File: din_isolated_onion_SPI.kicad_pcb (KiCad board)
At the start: 2 copper layers, 32.5 x 40.5 mm, 38 parts, among them J1 Conn_01x16, J2 Conn_01x16, J3 Conn_01x10, U1 Omega2+, U2 SI8661AB-B-IS1, U3 TPL5010-Q1, U4 74LVC125, U5 NL7SZ19

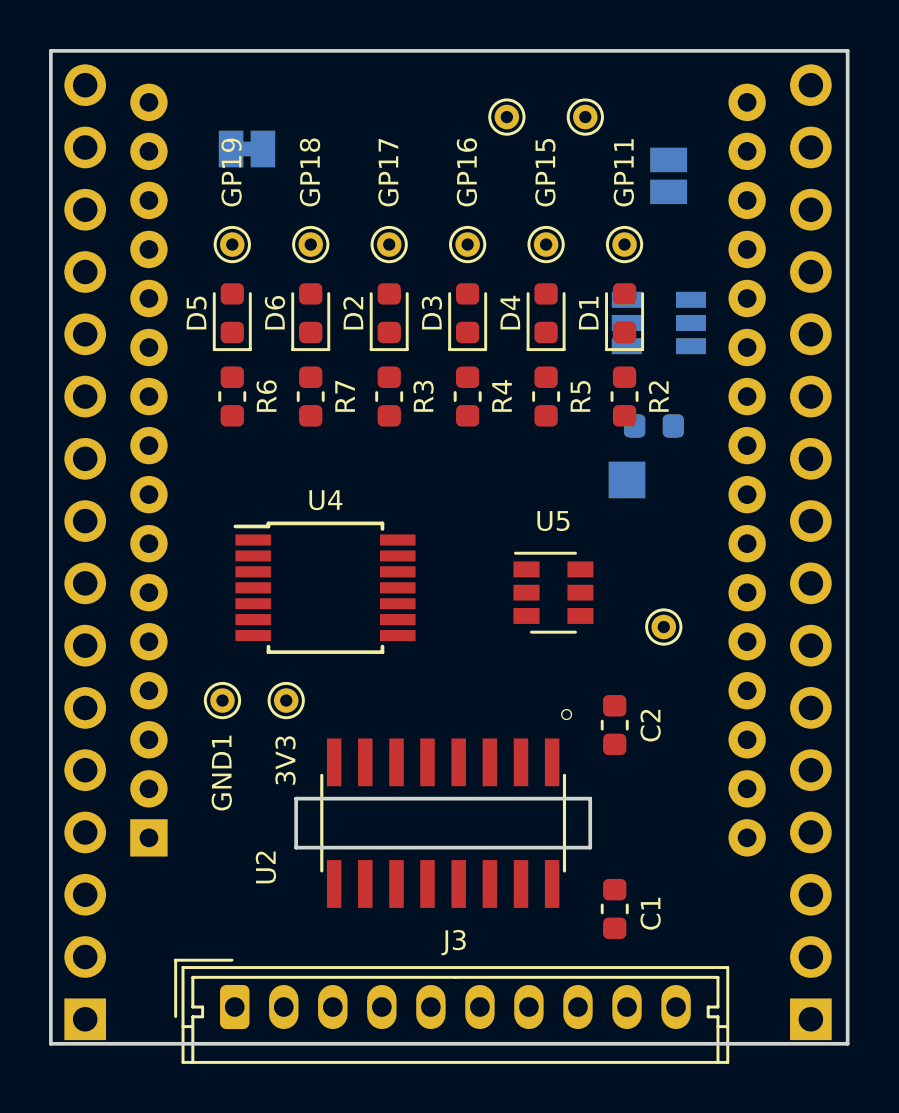
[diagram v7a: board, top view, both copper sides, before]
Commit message: Partially complete routing
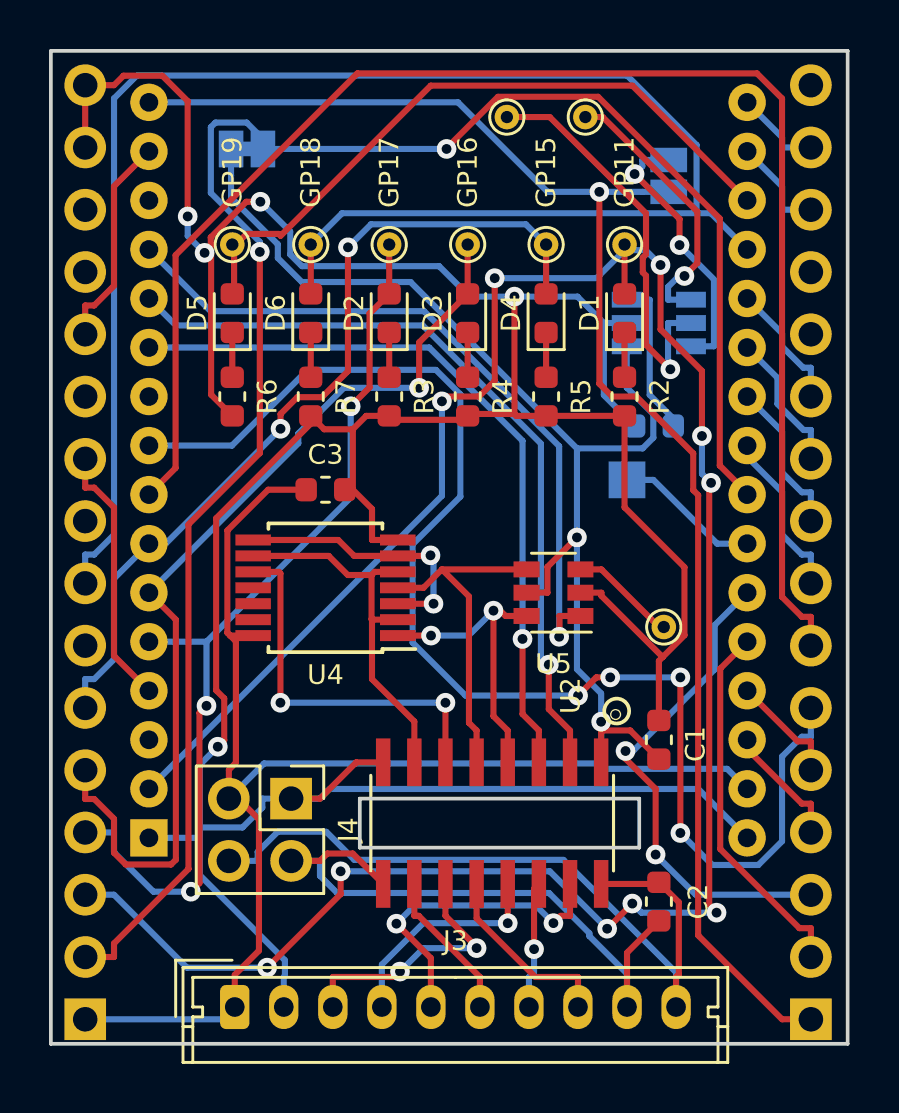
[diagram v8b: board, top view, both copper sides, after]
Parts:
- removed 3V3: TestPoint, TestPoint:TestPoint_THTPad_D1.0mm_Drill0.5mm
- removed GND1: GND, TestPoint:TestPoint_THTPad_D1.0mm_Drill0.5mm
- added C3: 100nF, Capacitor_SMD:C_0603_1608Metric, F.Cu at (141.2, 97.4)
- added J4: Test_Power_Bridge, Connector_PinHeader_2.54mm:PinHeader_2x02_P2.54mm_Vertical, F.Cu at (139.8, 110.0)
- moved C2 7.42 mm to (154.8, 114.2), turned to 270 degrees
- moved C1 7.13 mm to (154.8, 107.6)
- moved U2 2.00 mm to (148.0, 111.0)
- turned U4 to 180 degrees
- turned U5 to 180 degrees
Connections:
- U4 pad 1: CS0_O -> CSMUX_0
- U4 pad 10: CS2_O -> CS_SPARE
- U4 pad 4: CS1_O -> CSMUX_1
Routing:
- net GND_C: track 0.00 -> 147.6 mm, vias 0 -> 5
- net 3V3_C: track 0.00 -> 103.8 mm, vias 0 -> 2
- net /GP11: track 0.00 -> 95.3 mm, vias 0 -> 10
- net 3V3_O: track 0.00 -> 74.7 mm, vias 0 -> 2
- net /GP18: track 0.00 -> 69.5 mm
- net Net-(J2-Pad7): track 0.00 -> 61.5 mm
- net ~RST: track 0.00 -> 61.3 mm, vias 0 -> 1
- net Net-(J2-Pad6): track 0.00 -> 55.0 mm, vias 0 -> 4
- net /GP16: track 0.00 -> 39.6 mm, vias 0 -> 1
- net /GP17: track 0.00 -> 37.9 mm, vias 0 -> 3
- net /GP15: track 0.00 -> 35.3 mm, vias 0 -> 2
- net CLK_O: track 0.00 -> 31.9 mm, vias 0 -> 1
- net 3V3_I: track 0.00 -> 30.6 mm
- net MOSI_O: track 0.00 -> 30.2 mm, vias 0 -> 1
- net CS0_O: track 0.00 -> 29.5 mm, vias 0 -> 1
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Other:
- outline, holes or cut-outs redrawn
